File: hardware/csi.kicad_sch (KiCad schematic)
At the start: 1 part, among them J5 Conn_01x22_Female

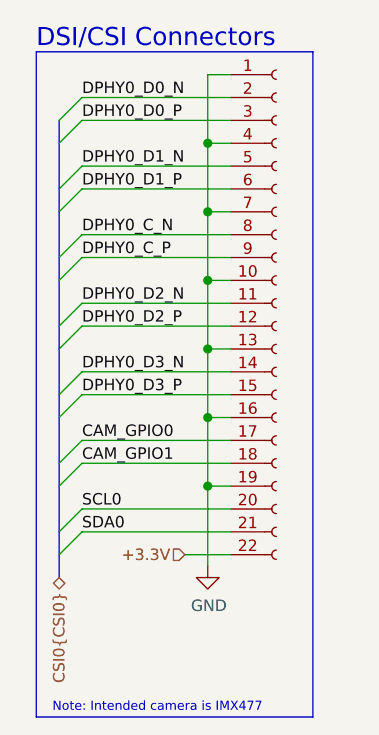
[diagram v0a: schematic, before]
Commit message: Fix schematic connectivity and add flashing access
The camera and Ethernet buses now connect across sheets: they use
unnamed bus groups so the member nets keep their names. Ethernet pair 2
negative is no longer tied to GND.

The RP2354A core supply reaches the regulator output, and a 12 MHz
crystal drives XIN/XOUT, which USB and the USB bootloader need. The
CM5 gets GPIO_VREF on 3.3 V, the IO Board's boot and EEPROM jumper
header, and a data-only USB-C port with 5.1 kOhm CC resistors for
flashing the eMMC.

Co-Authored-By: Claude Opus 5.5 <noreply@anthropic.com>
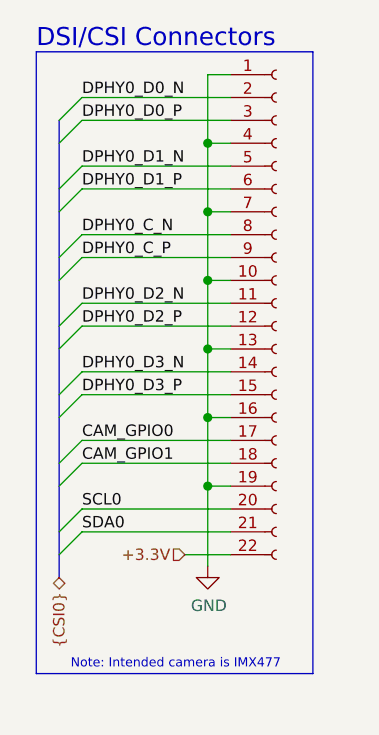
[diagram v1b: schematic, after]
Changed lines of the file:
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@@
 	(rectangle
 		(start 15.24 17.78)
-		(end 45.974 91.694)
+		(end 45.974 86.868)
 		(stroke
 			(width 0)
@@
 	(text "Note: Intended camera is IMX477"
 		(exclude_from_sim no)
-		(at 28.702 90.678 0)
+		(at 30.734 85.852 0)
 		(effects
 			(font
@@
 		)
 	)
-	(hierarchical_label "CSI0{CSI0}"
+	(hierarchical_label "{CSI0}"
 		(shape bidirectional)
 		(at 17.78 76.2 270)
